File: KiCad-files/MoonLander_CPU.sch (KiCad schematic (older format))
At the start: 17 parts, among them IC5 LPC824M201JHI33, J1 Cortex_JTAG/SWD_10, Y1 Crystal

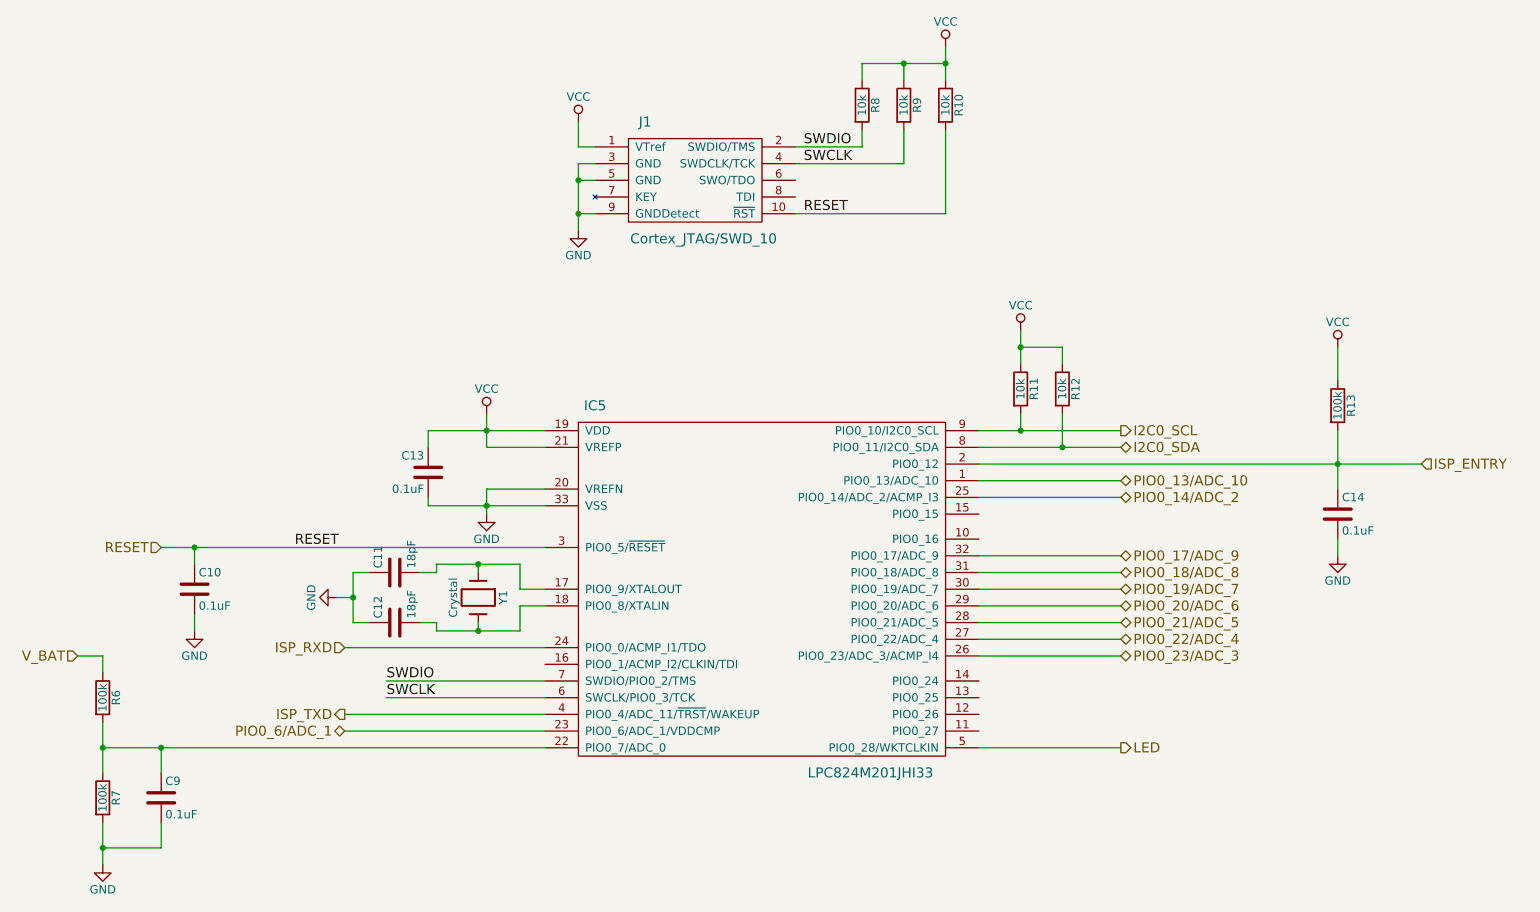
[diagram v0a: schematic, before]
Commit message: added I2C EEPROM, redid ground stitching
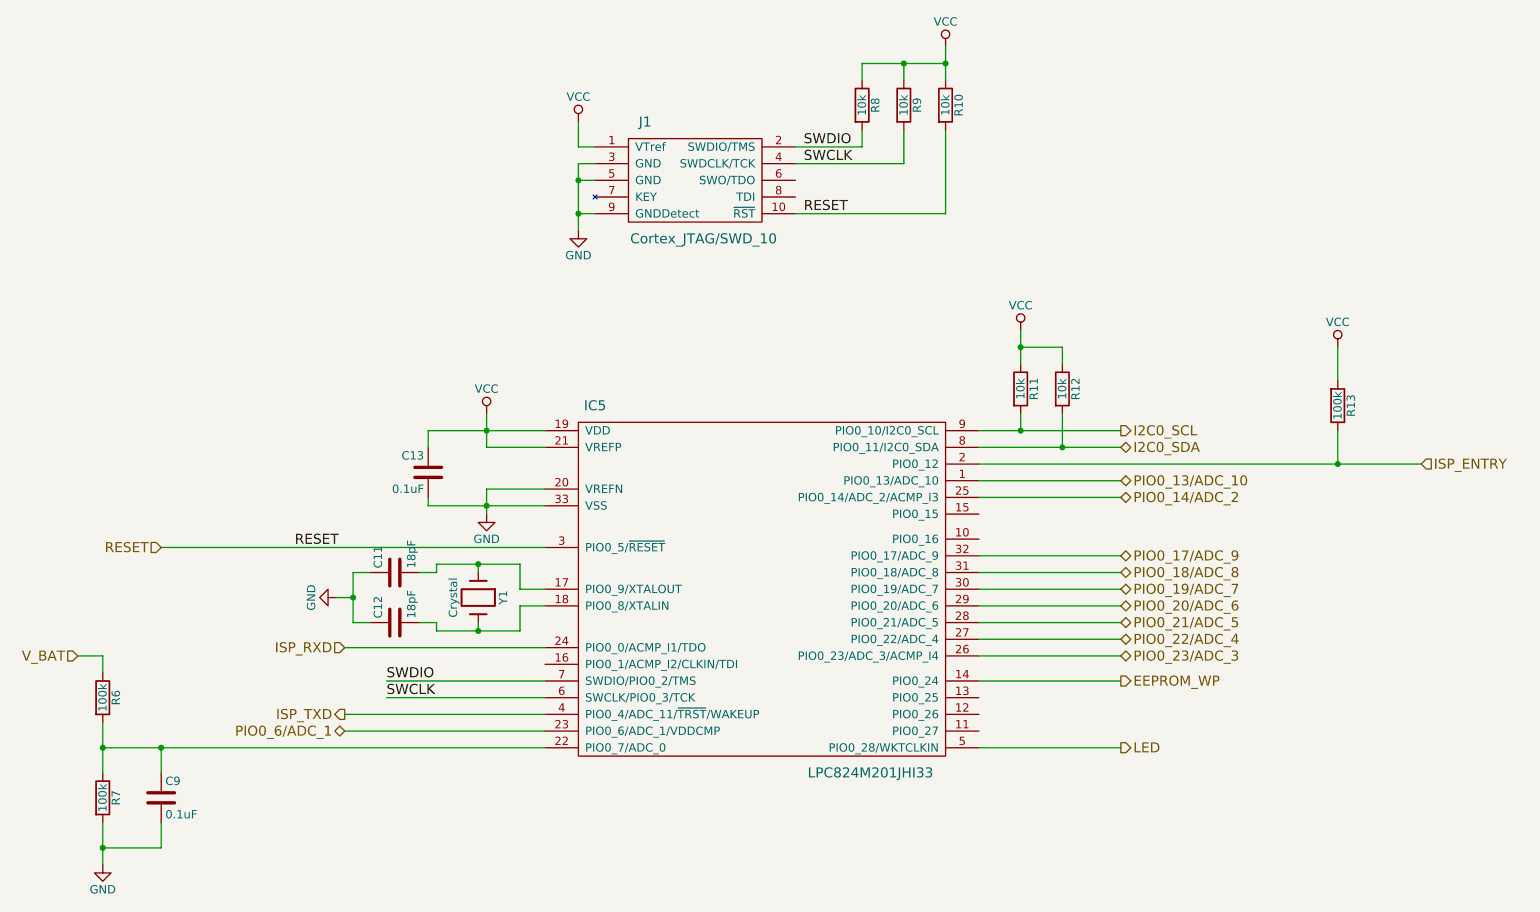
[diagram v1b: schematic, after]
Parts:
- removed C10, C14: 0.1uF, Capacitors_SMD:C_0402, symbol C
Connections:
- net ISP_ENTRY: now also R13.1; no longer R13.2
- net VCC: now also R13.2; no longer R13.1
- net EEPROM_WP: now reaches IC5.14 (PIO0_24)
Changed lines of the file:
@@
 $EndComp
 $Comp
-L VCC #PWR25
+L VCC #PWR9
 U 1 1 565F2E16
 P 3950 3250
-F 0 "#PWR25" H 3950 3100 50  0001 C CNN
+F 0 "#PWR9" H 3950 3100 50  0001 C CNN
 F 1 "VCC" H 3950 3400 50  0000 C CNN
 F 2 "" H 3950 3250 50  0000 C CNN
@@
 $EndComp
 $Comp
-L GND #PWR26
+L GND #PWR10
 U 1 1 565F2E2E
 P 3950 3850
-F 0 "#PWR26" H 3950 3600 50  0001 C CNN
+F 0 "#PWR10" H 3950 3600 50  0001 C CNN
 F 1 "GND" H 3950 3700 50  0000 C CNN
 F 2 "" H 3950 3850 50  0000 C CNN
@@
 $EndComp
 $Comp
-L VCC #PWR29
+L VCC #PWR22
 U 1 1 565F3B82
 P 6700 1050
-F 0 "#PWR29" H 6700 900 50  0001 C CNN
+F 0 "#PWR22" H 6700 900 50  0001 C CNN
 F 1 "VCC" H 6700 1200 50  0000 C CNN
 F 2 "" H 6700 1050 50  0000 C CNN
@@
 $EndComp
 $Comp
-L VCC #PWR27
+L VCC #PWR11
 U 1 1 565F3C33
 P 4500 1500
-F 0 "#PWR27" H 4500 1350 50  0001 C CNN
+F 0 "#PWR11" H 4500 1350 50  0001 C CNN
 F 1 "VCC" H 4500 1650 50  0000 C CNN
 F 2 "" H 4500 1500 50  0000 C CNN
@@
 $EndComp
 $Comp
-L GND #PWR28
+L GND #PWR12
 U 1 1 565F3C7E
 P 4500 2150
-F 0 "#PWR28" H 4500 1900 50  0001 C CNN
+F 0 "#PWR12" H 4500 1900 50  0001 C CNN
 F 1 "GND" H 4500 2000 50  0000 C CNN
 F 2 "" H 4500 2150 50  0000 C CNN
@@
 $EndComp
 $Comp
-L GND #PWR24
+L GND #PWR5
 U 1 1 565F4D06
 P 3050 4350
-F 0 "#PWR24" H 3050 4100 50  0001 C CNN
+F 0 "#PWR5" H 3050 4100 50  0001 C CNN
 F 1 "GND" H 3050 4200 50  0000 C CNN
 F 2 "" H 3050 4350 50  0000 C CNN
@@
 I2C0_SDA
 $Comp
-L VCC #PWR30
+L VCC #PWR24
 U 1 1 565F57DE
 P 7150 2750
-F 0 "#PWR30" H 7150 2600 50  0001 C CNN
+F 0 "#PWR24" H 7150 2600 50  0001 C CNN
 F 1 "VCC" H 7150 2900 50  0000 C CNN
 F 2 "" H 7150 2750 50  0000 C CNN
@@
 Wire Wire Line
 	6900 3550 9550 3550
-Wire Wire Line
-	9050 3350 9050 3700
 $Comp
 L R R13
@@
 F 3 "" H 9050 3200 50  0000 C CNN
 	1    9050 3200
-	1    0    0    -1
+	1    0    0    1
 $EndComp
 Wire Wire Line
@@
 	7400 2850 7150 2850
 $Comp
-L VCC #PWR31
+L VCC #PWR28
 U 1 1 565F82A6
 P 9050 2850
-F 0 "#PWR31" H 9050 2700 50  0001 C CNN
+F 0 "#PWR28" H 9050 2700 50  0001 C CNN
 F 1 "VCC" H 9050 3000 50  0000 C CNN
 F 2 "" H 9050 2850 50  0000 C CNN
@@
 $EndComp
 $Comp
-L GND #PWR22
+L GND #PWR1
 U 1 1 565FF956
 P 1650 5950
-F 0 "#PWR22" H 1650 5700 50  0001 C CNN
+F 0 "#PWR1" H 1650 5700 50  0001 C CNN
 F 1 "GND" H 1650 5800 50  0000 C CNN
 F 2 "" H 1650 5950 50  0000 C CNN
@@
 	2000 5250 2000 5400
 Connection ~ 2000 5250
-$Comp
-L C C14
-U 1 1 56610699
-P 9050 3850
-F 0 "C14" H 9075 3950 50  0000 L CNN
-F 1 "0.1uF" H 9075 3750 50  0000 L CNN
-F 2 "Capacitors_SMD:C_0402" H 9088 3700 50  0001 C CNN
-F 3 "" H 9050 3850 50  0000 C CNN
-	1    9050 3850
-	1    0    0    -1
-$EndComp
-$Comp
-L GND #PWR32
-U 1 1 56610766
-P 9050 4100
-F 0 "#PWR32" H 9050 3850 50  0001 C CNN
-F 1 "GND" H 9050 3950 50  0000 C CNN
-F 2 "" H 9050 4100 50  0000 C CNN
-F 3 "" H 9050 4100 50  0000 C CNN
-	1    9050 4100
-	1    0    0    -1
-$EndComp
-Wire Wire Line
-	9050 4100 9050 4000
 Text HLabel 2000 4050 0    60   Input ~ 0
 RESET
 Wire Wire Line
 	3600 3350 4300 3350
-$Comp
-L C C10
-U 1 1 566346FD
-P 2200 4300
-F 0 "C10" H 2225 4400 50  0000 L CNN
-F 1 "0.1uF" H 2225 4200 50  0000 L CNN
-F 2 "Capacitors_SMD:C_0402" H 2238 4150 50  0001 C CNN
-F 3 "" H 2200 4300 50  0000 C CNN
-	1    2200 4300
-	1    0    0    -1
-$EndComp
-$Comp
-L GND #PWR23
-U 1 1 56634895
-P 2200 4550
-F 0 "#PWR23" H 2200 4300 50  0001 C CNN
-F 1 "GND" H 2200 4400 50  0000 C CNN
-F 2 "" H 2200 4550 50  0000 C CNN
-F 3 "" H 2200 4550 50  0000 C CNN
-	1    2200 4550
-	1    0    0    -1
-$EndComp
-Wire Wire Line
-	2200 4450 2200 4550
-Wire Wire Line
-	2200 4150 2200 4050
-Connection ~ 2200 4050
 $Bitmap
 Pos 6250 7500
@@
 EndData
 $EndBitmap
+Wire Wire Line
+	6900 4850 7750 4850
+Text HLabel 7750 4850 2    60   Output ~ 0
+EEPROM_WP
+Wire Wire Line
+	9050 3350 9050 3550
 $EndSCHEMATC

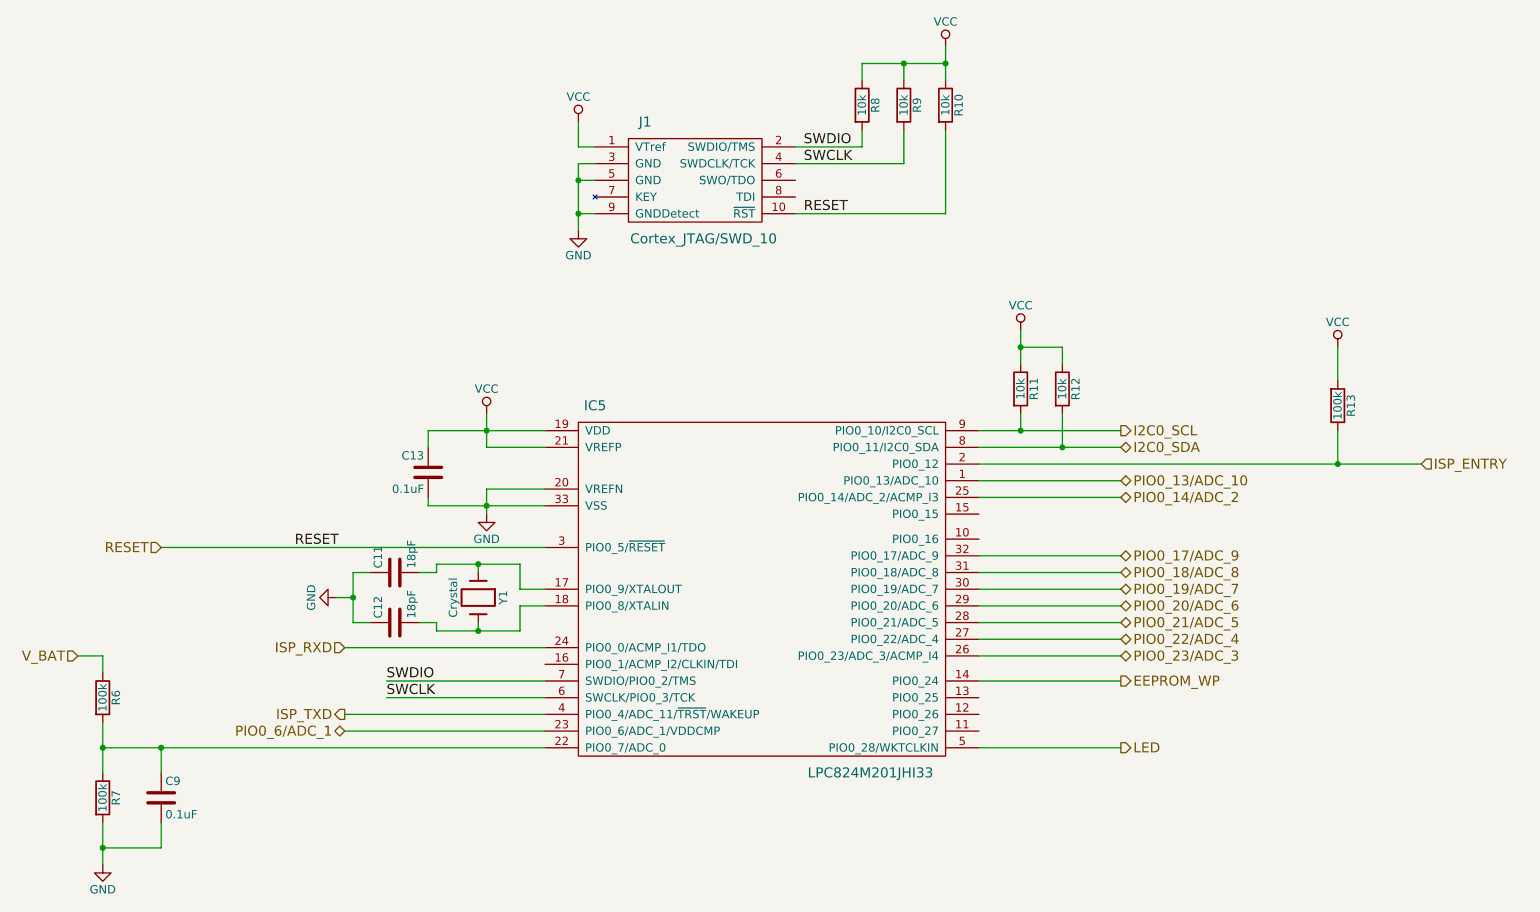
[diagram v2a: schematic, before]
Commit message: drive ISP_ENTRY and RST from CP2110 GPIO outputs
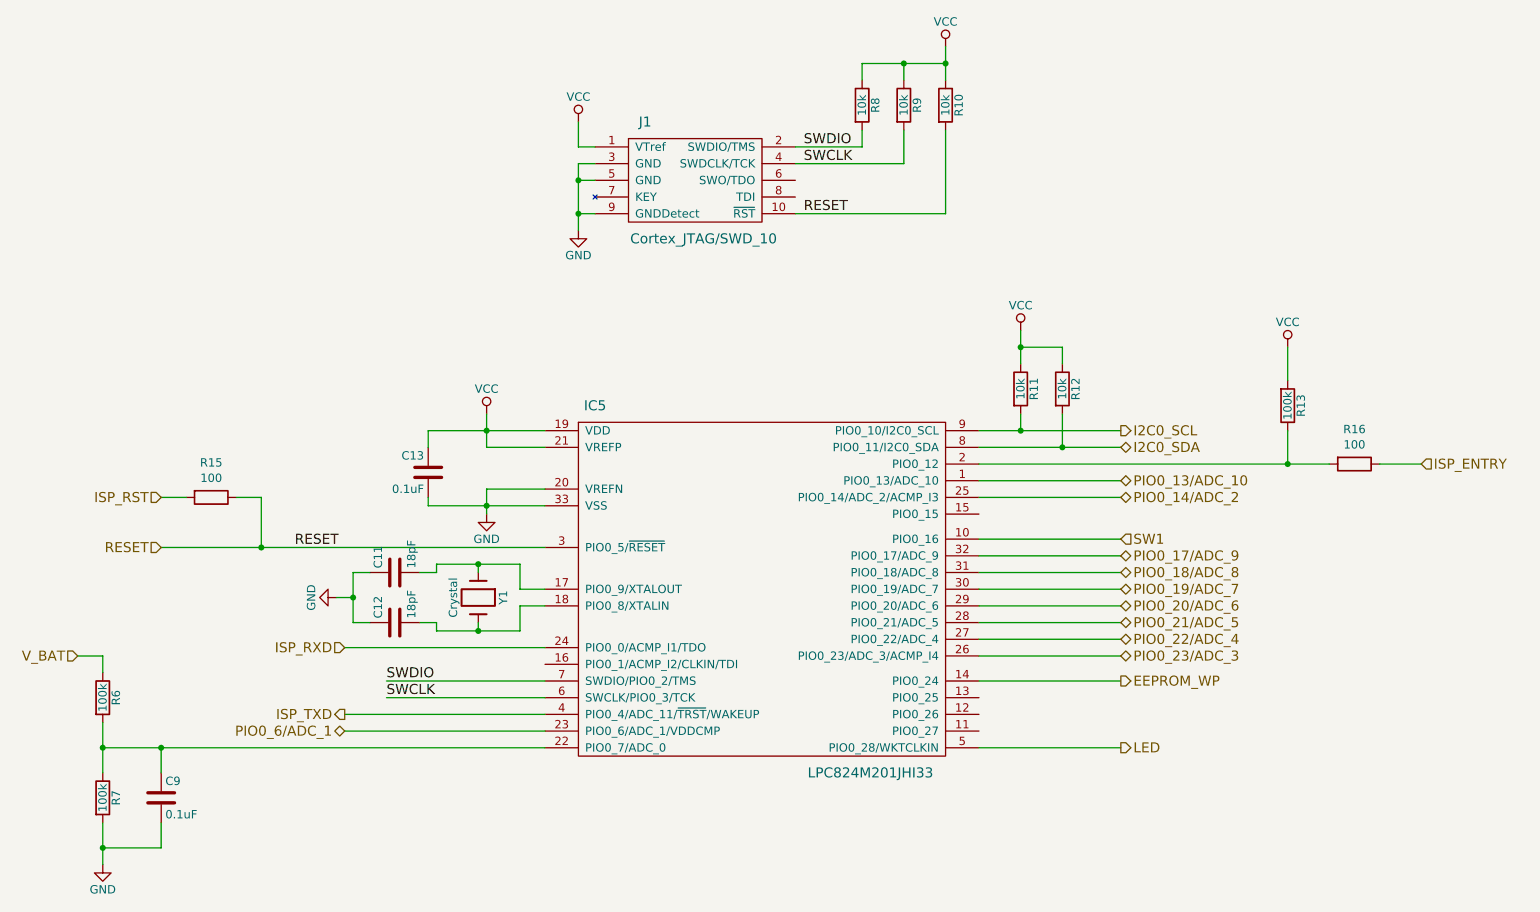
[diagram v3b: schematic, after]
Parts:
- added R15, R16: 100, Resistors_SMD:R_0402, symbol R
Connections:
- net ISP_ENTRY: now also R16.1; no longer IC5.2 (PIO0_12), R13.1
- net RESET: now also R15.1
- net SW1: now reaches IC5.10 (PIO0_16)
- new net: IC5.2 (PIO0_12), R13.1, R16.2
- new net ISP_RST: R15.2
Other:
- moved on the sheet: R13
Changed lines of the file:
@@
 $EndComp
 $Comp
-L VCC #PWR9
+L VCC #PWR8
 U 1 1 565F2E16
 P 3950 3250
-F 0 "#PWR9" H 3950 3100 50  0001 C CNN
+F 0 "#PWR8" H 3950 3100 50  0001 C CNN
 F 1 "VCC" H 3950 3400 50  0000 C CNN
 F 2 "" H 3950 3250 50  0000 C CNN
@@
 $EndComp
 $Comp
-L GND #PWR10
+L GND #PWR9
 U 1 1 565F2E2E
 P 3950 3850
-F 0 "#PWR10" H 3950 3600 50  0001 C CNN
+F 0 "#PWR9" H 3950 3600 50  0001 C CNN
 F 1 "GND" H 3950 3700 50  0000 C CNN
 F 2 "" H 3950 3850 50  0000 C CNN
@@
 $EndComp
 $Comp
-L VCC #PWR22
+L VCC #PWR21
 U 1 1 565F3B82
 P 6700 1050
-F 0 "#PWR22" H 6700 900 50  0001 C CNN
+F 0 "#PWR21" H 6700 900 50  0001 C CNN
 F 1 "VCC" H 6700 1200 50  0000 C CNN
 F 2 "" H 6700 1050 50  0000 C CNN
@@
 $EndComp
 $Comp
-L VCC #PWR11
+L VCC #PWR10
 U 1 1 565F3C33
 P 4500 1500
-F 0 "#PWR11" H 4500 1350 50  0001 C CNN
+F 0 "#PWR10" H 4500 1350 50  0001 C CNN
 F 1 "VCC" H 4500 1650 50  0000 C CNN
 F 2 "" H 4500 1500 50  0000 C CNN
@@
 $EndComp
 $Comp
-L GND #PWR12
+L GND #PWR11
 U 1 1 565F3C7E
 P 4500 2150
-F 0 "#PWR12" H 4500 1900 50  0001 C CNN
+F 0 "#PWR11" H 4500 1900 50  0001 C CNN
 F 1 "GND" H 4500 2000 50  0000 C CNN
 F 2 "" H 4500 2150 50  0000 C CNN
@@
 $EndComp
 $Comp
-L GND #PWR5
+L GND #PWR4
 U 1 1 565F4D06
 P 3050 4350
-F 0 "#PWR5" H 3050 4100 50  0001 C CNN
+F 0 "#PWR4" H 3050 4100 50  0001 C CNN
 F 1 "GND" H 3050 4200 50  0000 C CNN
 F 2 "" H 3050 4350 50  0000 C CNN
@@
 I2C0_SDA
 $Comp
-L VCC #PWR24
+L VCC #PWR23
 U 1 1 565F57DE
 P 7150 2750
-F 0 "#PWR24" H 7150 2600 50  0001 C CNN
+F 0 "#PWR23" H 7150 2600 50  0001 C CNN
 F 1 "VCC" H 7150 2900 50  0000 C CNN
 F 2 "" H 7150 2750 50  0000 C CNN
@@
 	6900 3650 7750 3650
 Wire Wire Line
-	6900 3550 9550 3550
+	6900 3550 9000 3550
 $Comp
 L R R13
 U 1 1 565F7CAC
-P 9050 3200
-F 0 "R13" V 9130 3200 50  0000 C CNN
-F 1 "100k" V 9050 3200 50  0000 C CNN
-F 2 "Resistors_SMD:R_0402" V 8980 3200 50  0001 C CNN
-F 3 "" H 9050 3200 50  0000 C CNN
-	1    9050 3200
+P 8750 3200
+F 0 "R13" V 8830 3200 50  0000 C CNN
+F 1 "100k" V 8750 3200 50  0000 C CNN
+F 2 "Resistors_SMD:R_0402" V 8680 3200 50  0001 C CNN
+F 3 "" H 8750 3200 50  0000 C CNN
+	1    8750 3200
 	1    0    0    1
 $EndComp
 Wire Wire Line
-	9050 2850 9050 3050
-Connection ~ 9050 3550
+	8750 2850 8750 3050
+Connection ~ 8750 3550
 Text HLabel 9550 3550 2    60   Input ~ 0
 ISP_ENTRY
@@
 	7400 2850 7150 2850
 $Comp
-L VCC #PWR28
+L VCC #PWR27
 U 1 1 565F82A6
-P 9050 2850
-F 0 "#PWR28" H 9050 2700 50  0001 C CNN
-F 1 "VCC" H 9050 3000 50  0000 C CNN
-F 2 "" H 9050 2850 50  0000 C CNN
-F 3 "" H 9050 2850 50  0000 C CNN
-	1    9050 2850
+P 8750 2850
+F 0 "#PWR27" H 8750 2700 50  0001 C CNN
+F 1 "VCC" H 8750 3000 50  0000 C CNN
+F 2 "" H 8750 2850 50  0000 C CNN
+F 3 "" H 8750 2850 50  0000 C CNN
+	1    8750 2850
 	1    0    0    -1
 $EndComp
@@
 03 43 83 61 8C 09 03 03 03 03 43 83 61 8C 09 03 03 03 03 43 83 61 8C 09 03 03 03 03 43 83 61 03
 60 D2 64 32 30 30 30 30 34 84 CF 1C 00 A9 00 9C 01 A8 8B 59 19 06 06 06 06 06 E9 E3 33 80 C5 FF
-07 47 25 A5 D2 E9 03 52 D8 00 00 00 00 49 45 4E 44 AE 42 60 82 00
+07 47 25 A5 D2 E9 03 52 D8 00 00 00 00 49 45 4E 44 AE 42 60 82 7F
 EndData
 $EndBitmap
@@
 EEPROM_WP
 Wire Wire Line
-	9050 3350 9050 3550
+	8750 3550 8750 3350
+Text HLabel 7750 4000 2    60   Input ~ 0
+SW1
+Wire Wire Line
+	7750 4000 6900 4000
+$Comp
+L R R16
+U 1 1 56B52176
+P 9150 3550
+F 0 "R16" V 8942 3550 50  0000 C CNN
+F 1 "100" V 9034 3550 50  0000 C CNN
+F 2 "Resistors_SMD:R_0402" V 9080 3550 50  0001 C CNN
+F 3 "" H 9150 3550 50  0000 C CNN
+	1    9150 3550
+	0    1    1    0
+$EndComp
+Wire Wire Line
+	9300 3550 9550 3550
+$Comp
+L R R15
+U 1 1 56B522FC
+P 2300 3750
+F 0 "R15" V 2092 3750 50  0000 C CNN
+F 1 "100" V 2184 3750 50  0000 C CNN
+F 2 "Resistors_SMD:R_0402" V 2230 3750 50  0001 C CNN
+F 3 "" H 2300 3750 50  0000 C CNN
+	1    2300 3750
+	0    1    1    0
+$EndComp
+Wire Wire Line
+	2450 3750 2600 3750
+Wire Wire Line
+	2600 3750 2600 4050
+Connection ~ 2600 4050
+Text HLabel 2000 3750 0    60   Input ~ 0
+ISP_RST
+Wire Wire Line
+	2000 3750 2150 3750
 $EndSCHEMATC
